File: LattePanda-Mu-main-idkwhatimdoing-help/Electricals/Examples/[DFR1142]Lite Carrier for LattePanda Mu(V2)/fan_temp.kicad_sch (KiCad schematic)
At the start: 23 parts, among them M1 Fan_4pin, M2 Fan_4pin

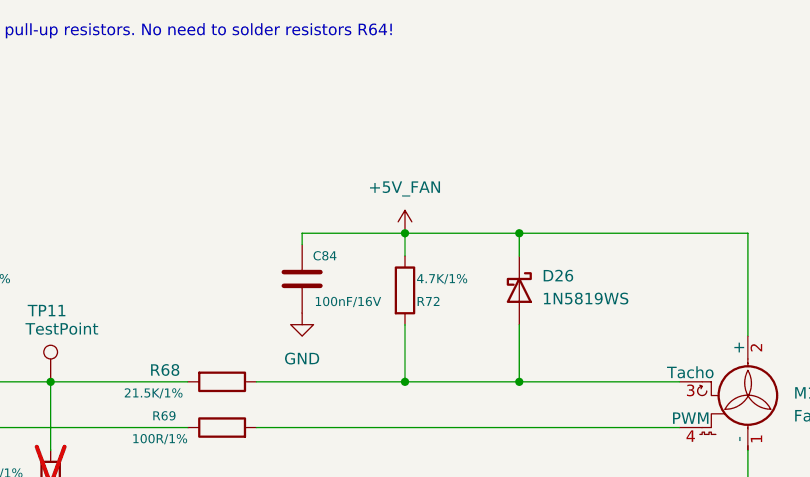
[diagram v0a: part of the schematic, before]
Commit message: Gave each screen a seperate backlight controller (different nit brightness)
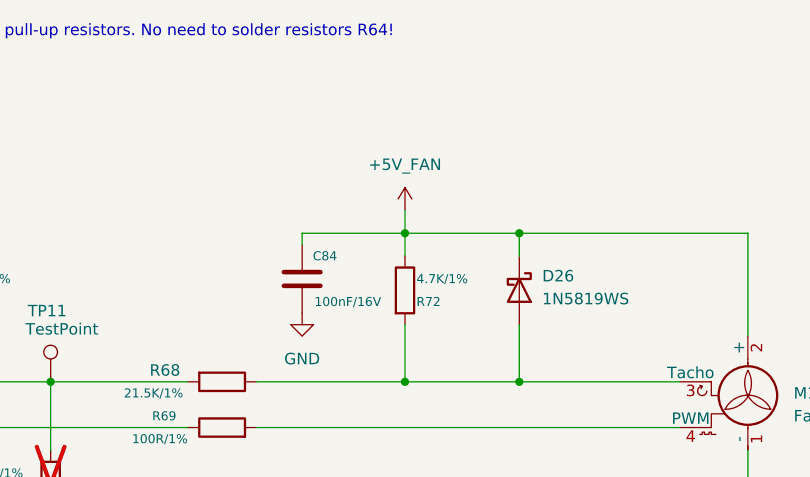
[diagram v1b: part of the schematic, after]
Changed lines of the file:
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@@
 	(wire
 		(pts
+			(xy 353.06 143.51) (xy 353.06 146.05)
+		)
+		(stroke
+			(width 0)
+			(type default)
+		)
+	)
+	(wire
+		(pts
 			(xy 226.06 146.05) (xy 226.06 148.59)
 		)
@@
 	(symbol
 		(lib_id "power:+5V")
-		(at 353.06 146.05 0)
+		(at 353.06 143.51 0)
 		(unit 1)
 		(body_style 1)
@@
 		(fields_autoplaced yes)
 		(property "Reference" "#PWR0135"
-			(at 353.06 149.86 0)
+			(at 353.06 147.32 0)
 			(hide yes)
 			(show_name no)
@@
 		)
 		(property "Value" "+5V_FAN"
-			(at 353.06 140.97 0)
+			(at 353.06 138.43 0)
 			(show_name no)
 			(do_not_autoplace no)
@@
 		)
 		(property "Footprint" ""
-			(at 353.06 146.05 0)
+			(at 353.06 143.51 0)
 			(hide yes)
 			(show_name no)
@@
 		)
 		(property "Datasheet" ""
-			(at 353.06 146.05 0)
+			(at 353.06 143.51 0)
 			(hide yes)
 			(show_name no)
@@
 		)
 		(property "Description" ""
-			(at 353.06 146.05 0)
+			(at 353.06 143.51 0)
 			(hide yes)
 			(show_name no)
@@
 		)
 		(property "无标题字段" ""
-			(at 353.06 146.05 0)
+			(at 353.06 143.51 0)
 			(hide yes)
 			(show_name no)
